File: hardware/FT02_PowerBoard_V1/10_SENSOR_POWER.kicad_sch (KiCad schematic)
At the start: 0 parts

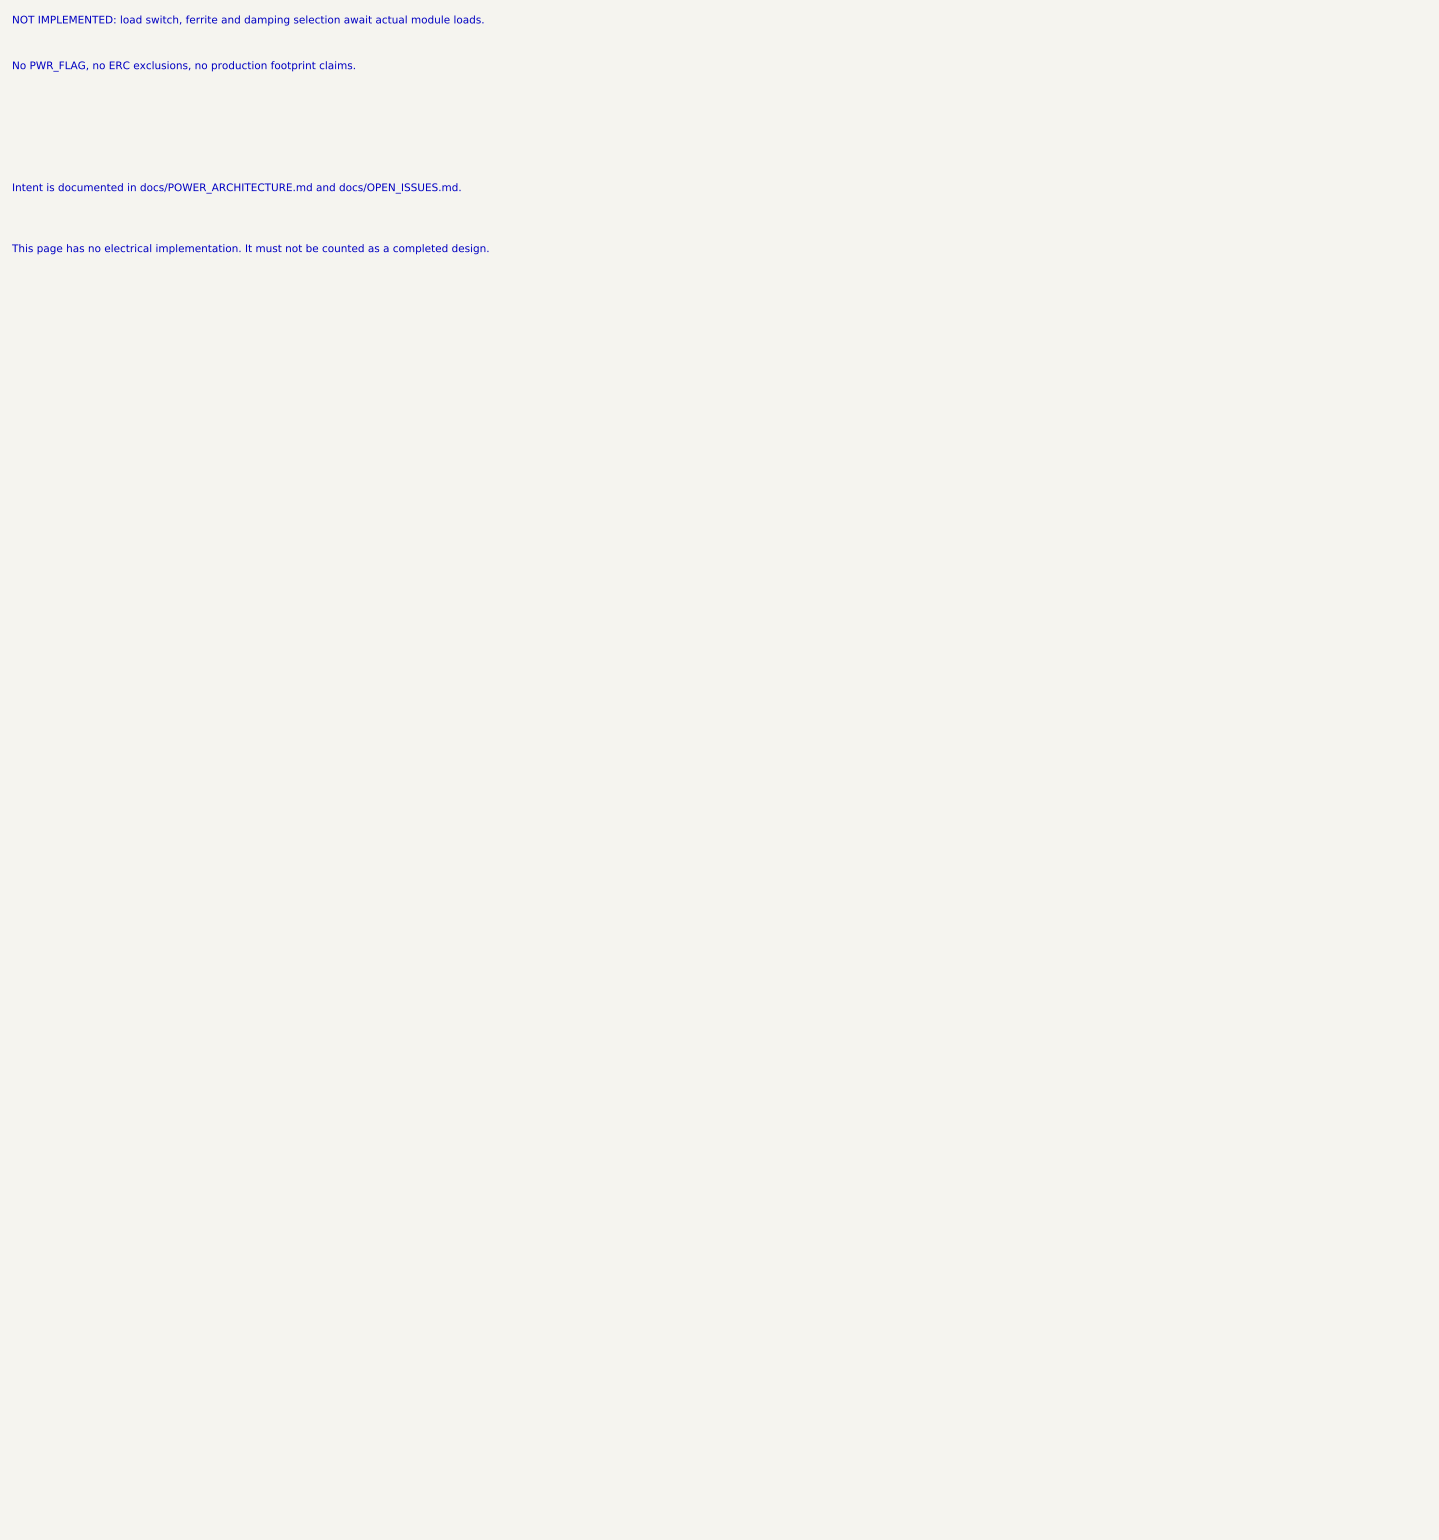
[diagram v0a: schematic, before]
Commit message: Wire FT02 Phase 1 power stages and verify partial shunt boundary
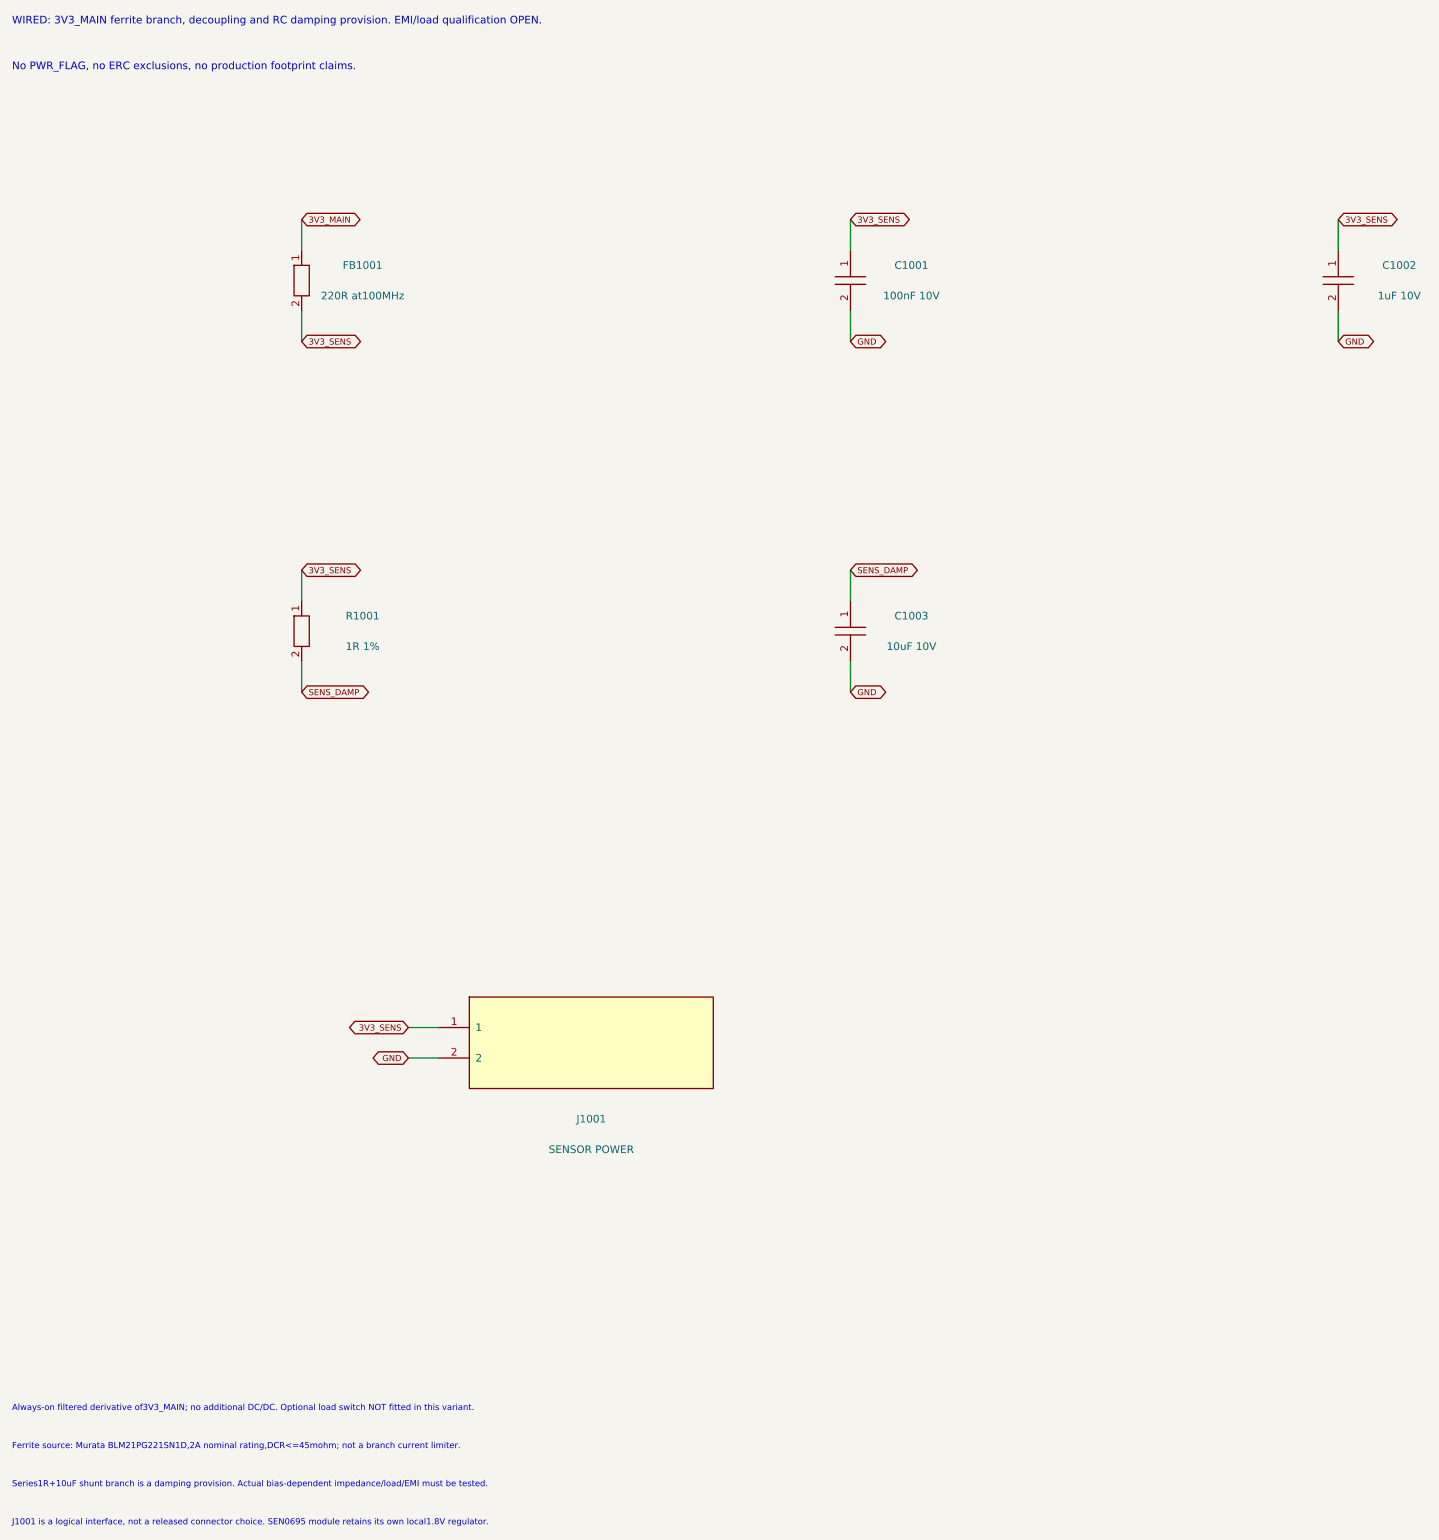
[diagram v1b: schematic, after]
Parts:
- added C1001: 100nF 10V, symbol FT02_Reference:C
- added C1002: 1uF 10V, symbol FT02_Reference:C
- added C1003: 10uF 10V, symbol FT02_Reference:C
- added FB1001: 220R at100MHz, symbol FT02_Reference:R
- added J1001: SENSOR POWER, symbol FT02_Reference:CONN2
- added R1001: 1R 1%, symbol FT02_Reference:R
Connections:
- new net 3V3_MAIN: FB1001.1
- new net 3V3_SENS: C1001.1, C1002.1, FB1001.2, J1001.1, R1001.1
- new net GND: C1001.2, C1002.2, C1003.2, J1001.2
- new net SENS_DAMP: C1003.1, R1001.2
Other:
- note added: "Always-on filtered derivative of3V3_MAIN; no additional DC/DC. Optional load switch NOT fitted in this variant."
- note added: "Ferrite source: Murata BLM21PG221SN1D,2A nominal rating,DCR<=45mohm; not a branch current limiter."
- note added: "J1001 is a logical interface, not a released connector choice. SEN0695 module retains its own local1.8V regulator."
- note added: "Series1R+10uF shunt branch is a damping provision. Actual bias-dependent impedance/load/EMI must be tested."
- note added: "WIRED: 3V3_MAIN ferrite branch, decoupling and RC damping provision. EMI/load qualification OPEN."
- note removed: "Intent is documented in docs/POWER_ARCHITECTURE.md and docs/OPEN_ISSUES.md."
- note removed: "NOT IMPLEMENTED: load switch, ferrite and damping selection await actual module loads."
- note removed: "This page has no electrical implementation. It must not be counted as a completed design."
